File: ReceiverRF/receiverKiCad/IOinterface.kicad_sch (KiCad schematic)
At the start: 28 parts, among them Q1 MMBT3904, SW1 SW_Push, SW2 SW_Push, SW3 SW_Push, SW4 SW_Push

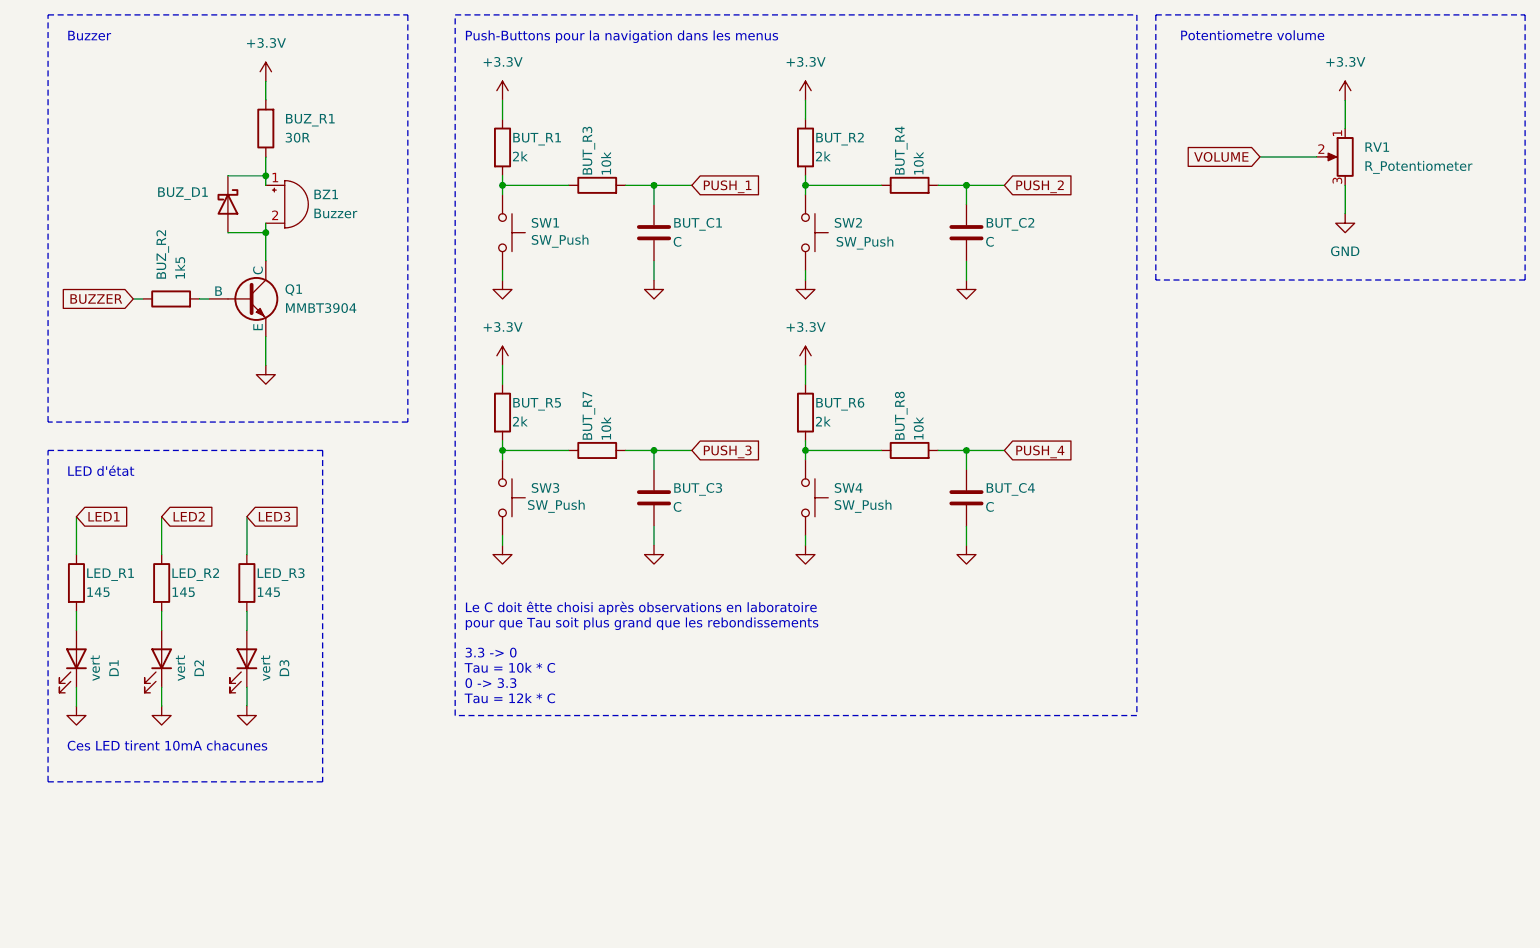
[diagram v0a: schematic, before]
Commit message: suggestions de Luca et placement sur PCB
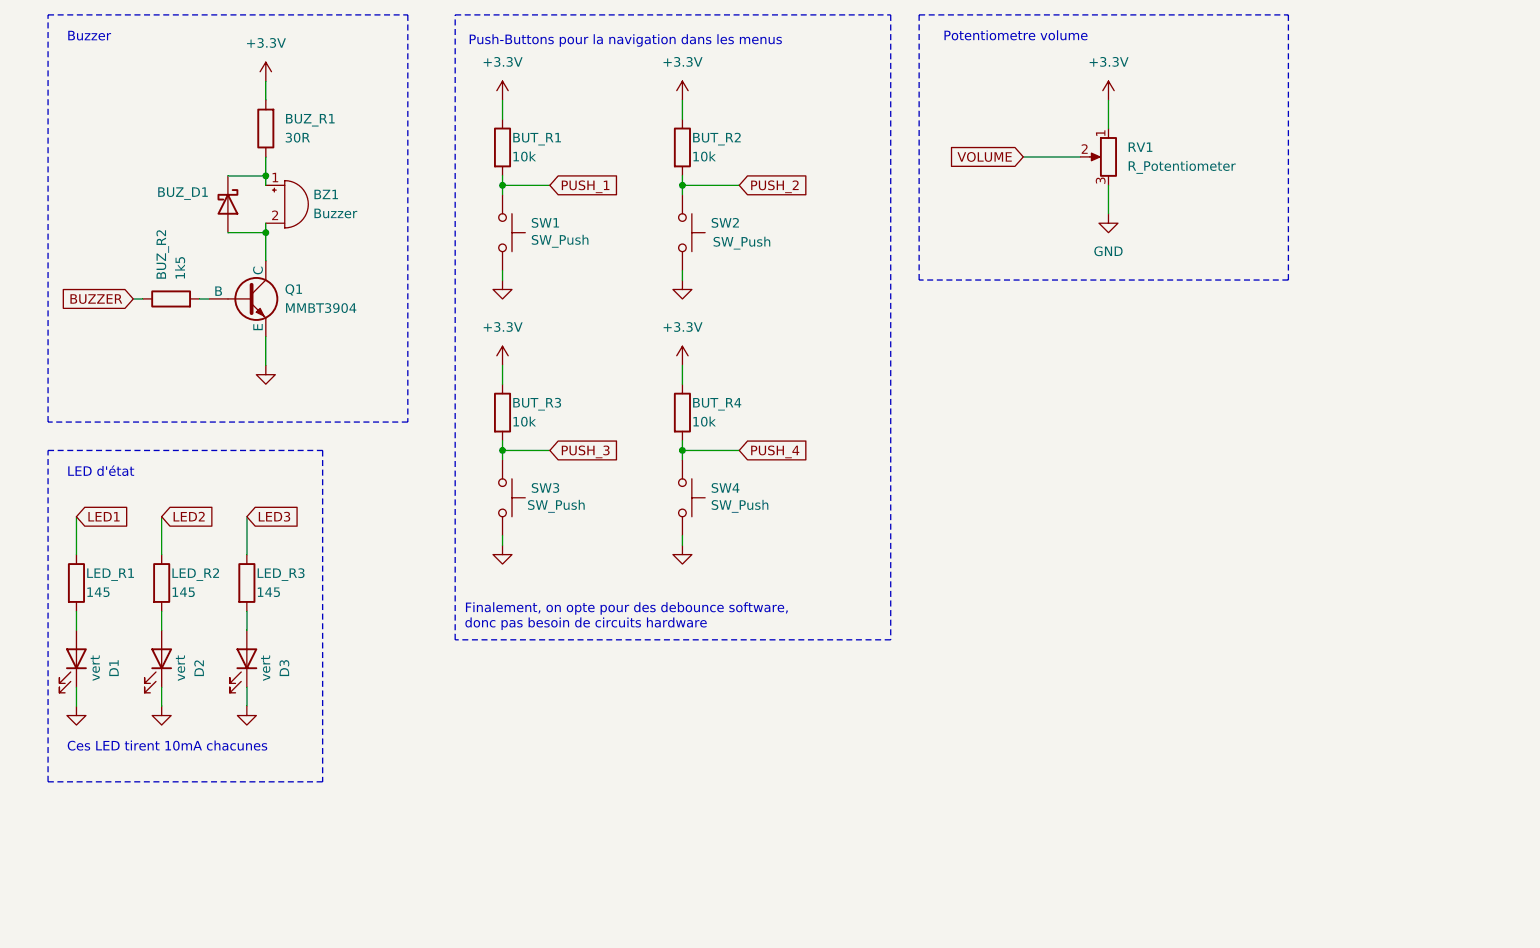
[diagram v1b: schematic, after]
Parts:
- removed BUT_C1, BUT_C2, BUT_C3, BUT_C4: C, Capacitor_SMD:C_0402_1005Metric, symbol Device:C
- removed BUT_R4, BUT_R7, BUT_R8: 10k, Resistor_SMD:R_0402_1005Metric, symbol Device:R
- removed BUT_R5: 2k, Resistor_SMD:R_0402_1005Metric, symbol Device:R
- BUT_R1, BUT_R2: value 2k -> 10k
- BUT_R4: renamed from BUT_R6; value 2k -> 10k
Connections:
- net +3.3V: now also BUT_R3.1
- net PUSH_1: now also BUT_R1.2, SW1.1; no longer BUT_R3.2
- net PUSH_2: now also BUT_R2.2, SW2.1
- net PUSH_3: now also BUT_R3.2, SW3.1
- net PUSH_4: now also BUT_R4.2, SW4.1
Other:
- note added: "Finalement, on opte pour des debounce software, donc pas besoin de circuits hardware"
- note removed: "3.3 -> 0 Tau = 10k * C 0 -> 3.3 Tau = 12k * C"
- note removed: "Le C doit êtte choisi après observations en laboratoire pour que Tau soit plus grand que les rebondissements"
- moved on the sheet: BUT_R2, BUT_R4, RV1, SW2, SW4

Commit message: aucun changement, simplement fichiers non sauvegardés du dernier commit
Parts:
- removed BUT_R3: 10k, Resistor_SMD:R_0402_1005Metric, symbol Device:R
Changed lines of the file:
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@@
-	(symbol
-		(lib_id "Device:R")
-		(at 83.82 74.93 0)
-		(unit 1)
-		(exclude_from_sim no)
-		(in_bom yes)
-		(on_board yes)
-		(dnp no)
-		(property "Reference" "BUT_R3"
-			(at 85.09 73.66 0)
-			(effects
-				(font
-					(size 1.27 1.27)
-				)
-				(justify left)
-			)
-		)
-		(property "Value" "10k"
-			(at 85.09 76.2 0)
-			(effects
-				(font
-					(size 1.27 1.27)
-				)
-				(justify left)
-			)
-		)
-		(property "Footprint" "Resistor_SMD:R_0402_1005Metric"
-			(at 82.042 74.93 90)
-			(effects
-				(font
-					(size 1.27 1.27)
-				)
-				(hide yes)
-			)
-		)
-		(property "Datasheet" "~"
-			(at 83.82 74.93 0)
-			(effects
-				(font
-					(size 1.27 1.27)
-				)
-				(hide yes)
-			)
-		)
-		(property "Description" ""
-			(at 83.82 74.93 0)
-			(effects
-				(font
-					(size 1.27 1.27)
-				)
-				(hide yes)
-			)
-		)
-		(pin "1"
-		)
-		(pin "2"
-		)
-		(instances
-			(project "receiver"
-				(path "/439ba515-58d4-4b14-87ab-b438dcf423a5/4d4f24f8-ecba-4dd7-9441-941d52592651"
-					(reference "BUT_R3")
-					(unit 1)
-				)
-			)
-		)
-	)
 	(symbol
 		(lib_id "Device:R")

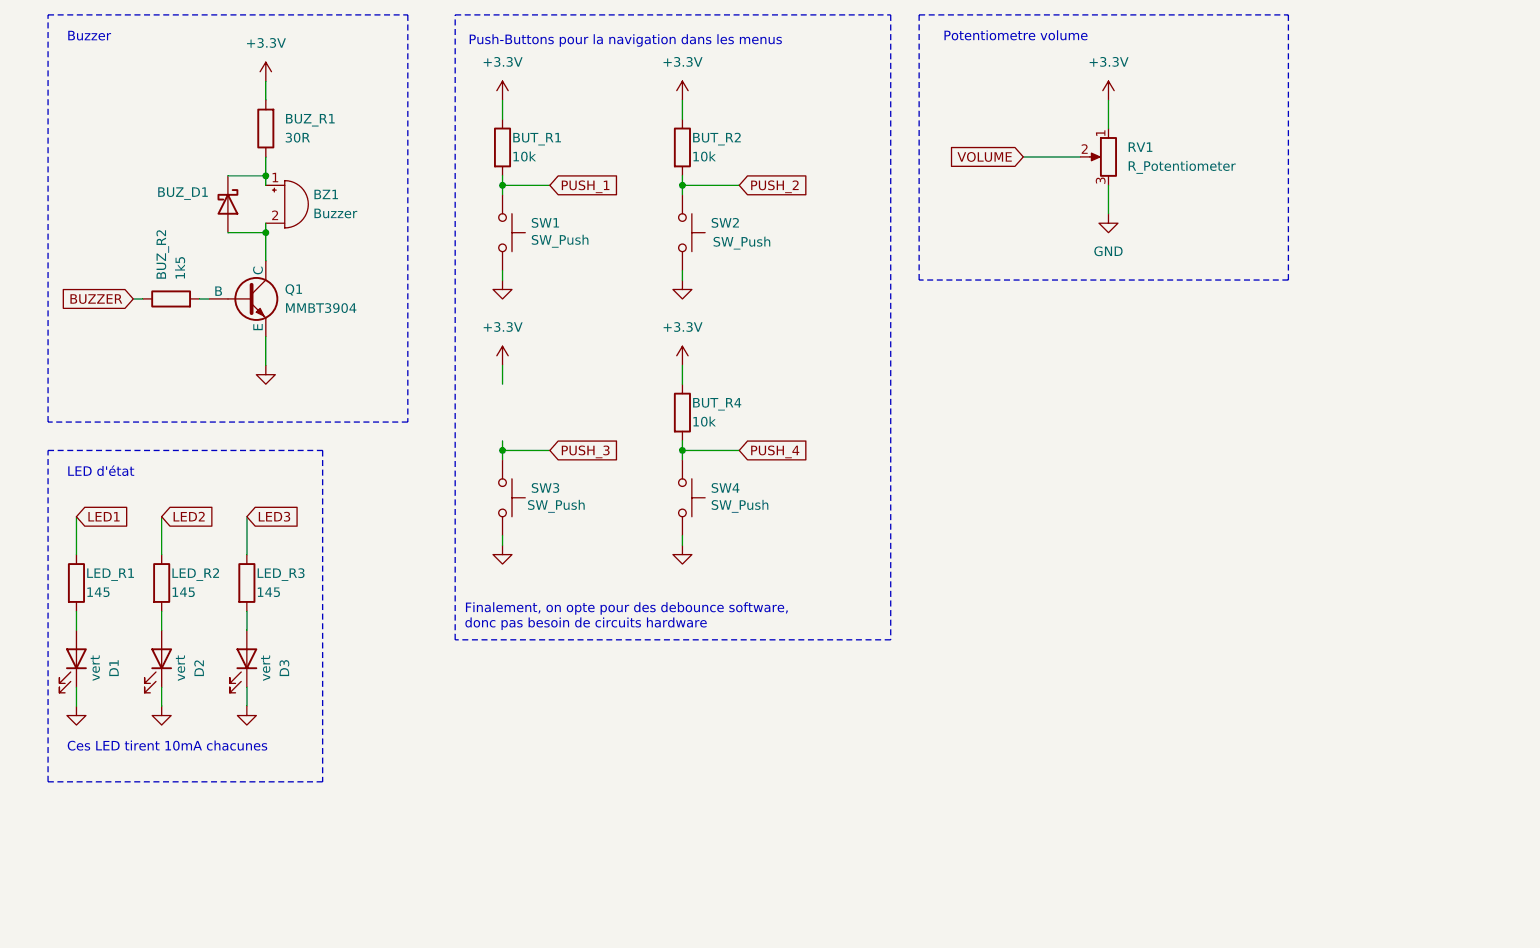
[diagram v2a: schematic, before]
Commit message: changement circuit volume du buzzer. Ajustement du volume direct plutot que software.
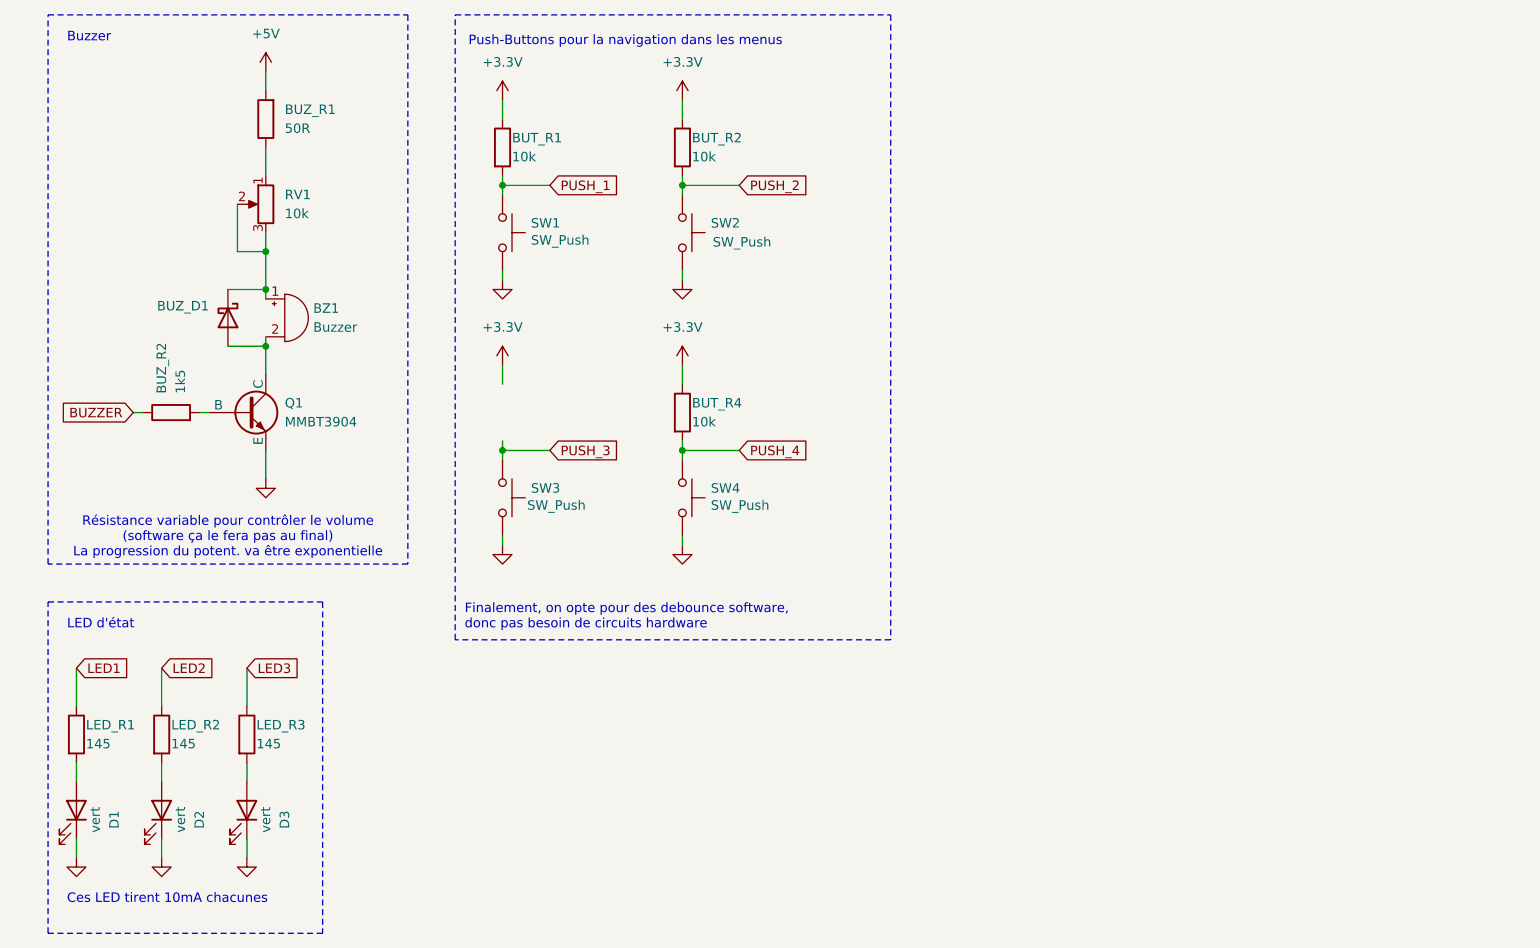
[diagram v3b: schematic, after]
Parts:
- BUZ_R1: value 30R -> 50R
- RV1: value R_Potentiometer -> 10k
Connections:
- net VOLUME is gone; now on an unnamed net: RV1.2
- net +3.3V: no longer BUZ_R1.2, RV1.1
- net GND: no longer RV1.3
- net at BUZ_D1.1 (K), BZ1.1 (-): now also RV1.3; no longer BUZ_R1.1
- new net: BUZ_R1.1, RV1.1
- new net +5V: BUZ_R1.2
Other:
- note added: "Résistance variable pour contrôler le volume (software ça le fera pas au final) La progression du potent. va être exponentielle"
- note removed: "Potentiometre volume"
- moved on the sheet: BUZ_D1, BUZ_R1, BUZ_R2, BZ1, D1, D2, D3, LED_R1, LED_R2, LED_R3, Q1, RV1
